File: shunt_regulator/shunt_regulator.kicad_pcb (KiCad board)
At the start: 2 copper layers, 87 x 94 mm, 58 parts, among them J1 Screw_Terminal_01x03, Q1 BC846B, Q2 BC846B, Q3 BC856B, Q4 30N06, U1 LM317_TO-252, U2 LM393

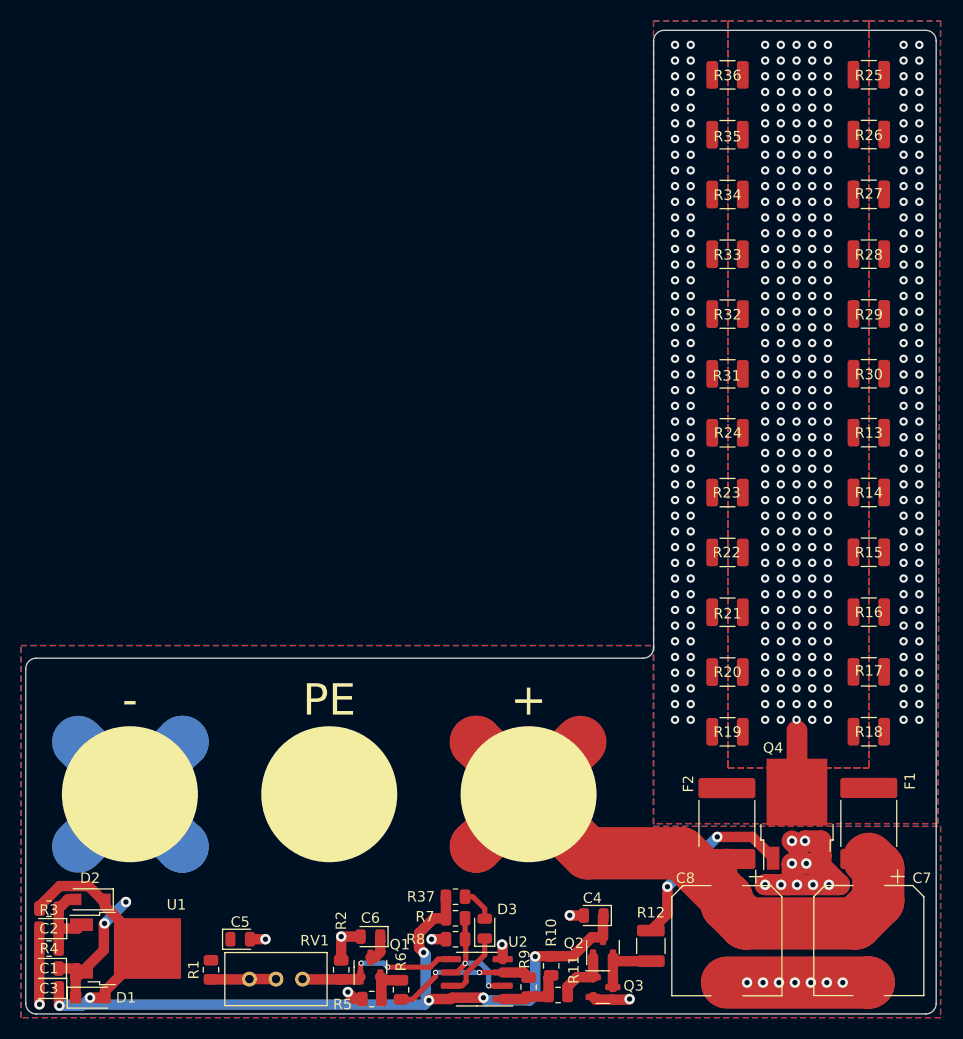
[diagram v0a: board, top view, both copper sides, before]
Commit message: Changed the power resistor footprint from 1210 to 2512
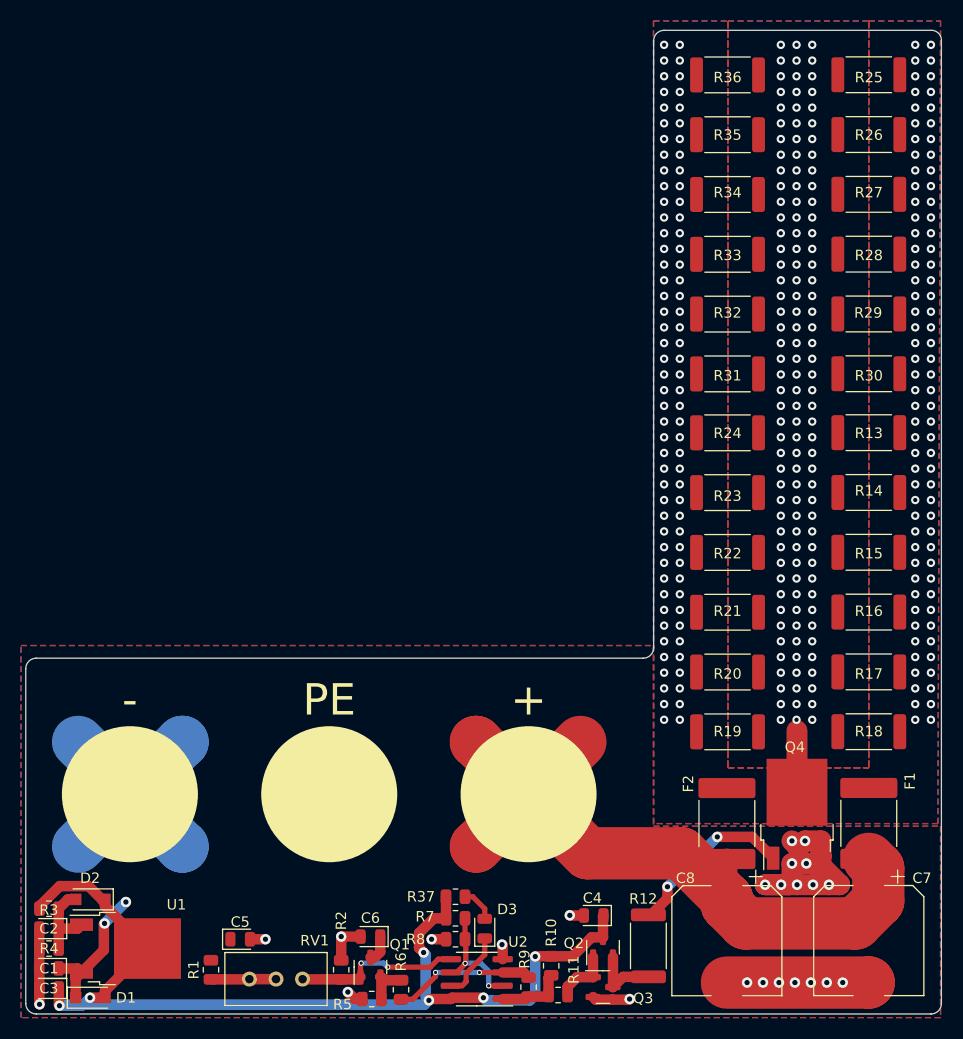
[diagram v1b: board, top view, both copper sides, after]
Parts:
- R12, R13, R14, R15, R16, R17, R18, R19, R20, R21, R22, R23, R24, R25, R26, R27, R28, R29, R30, R31, R32, R33, R34, R35, R36: footprint Resistor_SMD:R_1210_3225Metric -> Resistor_SMD:R_2512_6332Metric
- moved R12 0.23 mm to (30.5, 14.5)
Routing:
- net Net-(Q4-Pad1): track 17.8 -> 16.3 mm
- net Net-(Q4-Pad2): vias 220 -> 132
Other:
- board size 87 x 94 mm -> 87.5 x 94 mm
